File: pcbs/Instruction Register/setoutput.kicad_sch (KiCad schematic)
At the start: 9 parts, among them U3001 74HC245

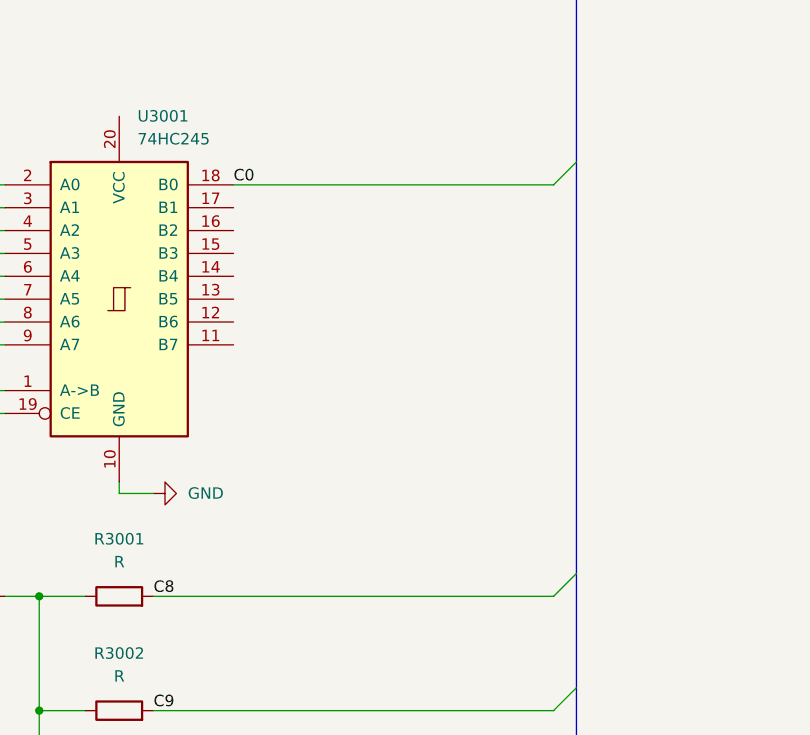
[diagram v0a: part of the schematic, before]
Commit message: Tweaking schematic and basic routing
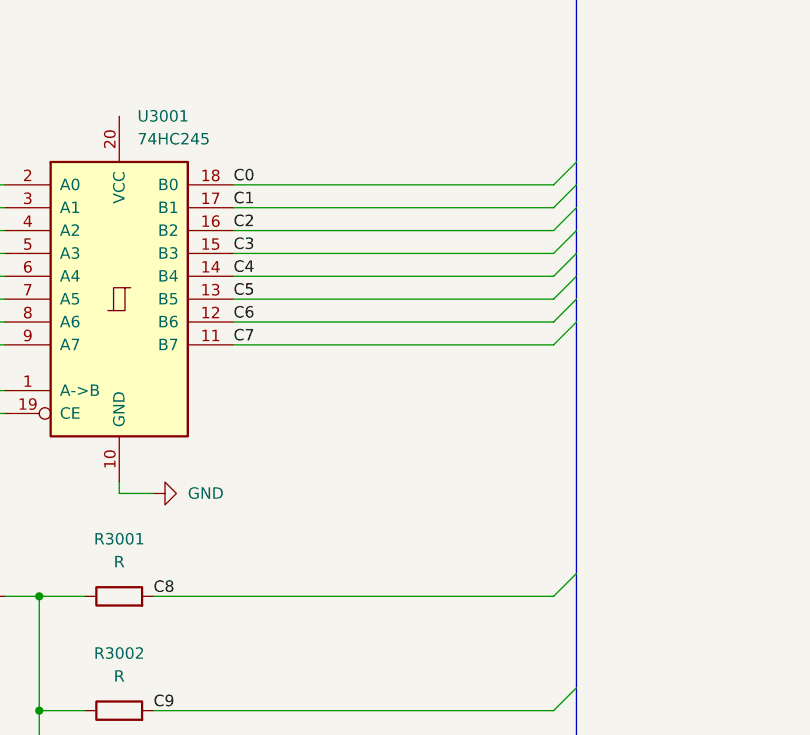
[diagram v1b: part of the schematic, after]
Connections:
- net C7: now reaches U3001.11 (B7)
- net C6: now reaches U3001.12 (B6)
- net C5: now reaches U3001.13 (B5)
- net C4: now reaches U3001.14 (B4)
- net C3: now reaches U3001.15 (B3)
- net C2: now reaches U3001.16 (B2)
- net C1: now reaches U3001.17 (B1)

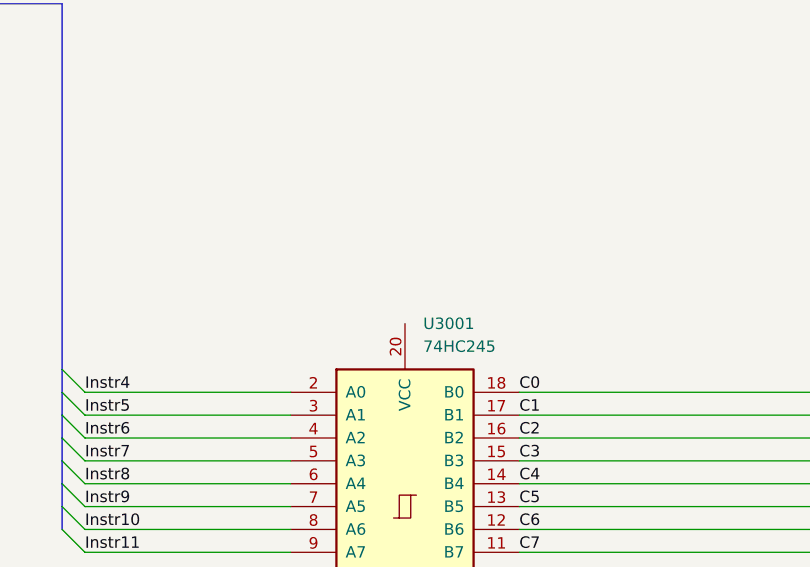
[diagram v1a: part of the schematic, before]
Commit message: Completing routing; needs silkscreen
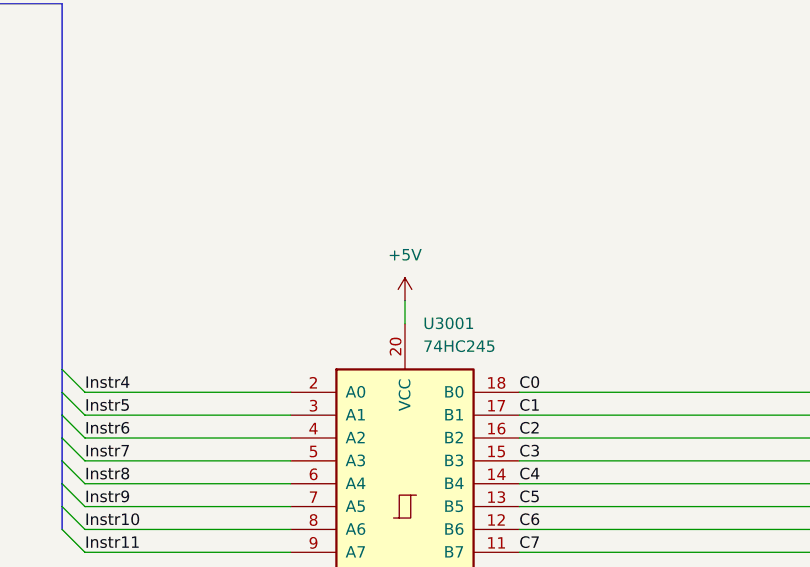
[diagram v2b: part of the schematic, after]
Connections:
- net +5V: now also U3001.20 (VCC)
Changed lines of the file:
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@@
+		)
+	)
+	(wire
+		(pts
+			(xy 127 83.82) (xy 127 86.36)
+		)
+		(stroke
+			(width 0)
+			(type default)
 		)
 	)
@@
 	(label "C4"
 		(at 139.7 104.14 0)
+		(fields_autoplaced yes)
 		(effects
 			(font
@@
 	(label "C5"
 		(at 139.7 106.68 0)
+		(fields_autoplaced yes)
 		(effects
 			(font
@@
 	(label "C2"
 		(at 139.7 99.06 0)
+		(fields_autoplaced yes)
 		(effects
 			(font
@@
 	(label "C1"
 		(at 139.7 96.52 0)
+		(fields_autoplaced yes)
 		(effects
 			(font
@@
 	(label "C3"
 		(at 139.7 101.6 0)
+		(fields_autoplaced yes)
 		(effects
 			(font
@@
 	(label "C7"
 		(at 139.7 111.76 0)
+		(fields_autoplaced yes)
 		(effects
 			(font
@@
 	(label "C6"
 		(at 139.7 109.22 0)
+		(fields_autoplaced yes)
 		(effects
 			(font
@@
 					(unit 1)
 				)
+			)
+		)
+	)
+	(symbol
+		(lib_id "power:+5V")
+		(at 127 83.82 0)
+		(unit 1)
+		(exclude_from_sim no)
+		(in_bom yes)
+		(on_board yes)
+		(dnp no)
+		(fields_autoplaced yes)
+		(property "Reference" "#PWR03004"
+			(at 127 87.63 0)
+			(effects
+				(font
+					(size 1.27 1.27)
+				)
+				(hide yes)
+			)
+		)
+		(property "Value" "+5V"
+			(at 127 78.74 0)
+			(effects
+				(font
+					(size 1.27 1.27)
+				)
+			)
+		)
+		(property "Footprint" ""
+			(at 127 83.82 0)
+			(effects
+				(font
+					(size 1.27 1.27)
+				)
+				(hide yes)
+			)
+		)
+		(property "Datasheet" ""
+			(at 127 83.82 0)
+			(effects
+				(font
+					(size 1.27 1.27)
+				)
+				(hide yes)
+			)
+		)
+		(property "Description" "Power symbol creates a global label with name \"+5V\""
+			(at 127 83.82 0)
+			(effects
+				(font
+					(size 1.27 1.27)
+				)
+				(hide yes)
+			)
+		)
+		(pin "1"
+		)
+		(instances
+			(project ""
+				(path "/dacc18b8-2bf2-4f24-ae04-b278bca3d46a/29957d29-df69-4b56-8517-df4781530091"
+					(reference "#PWR03004")
+					(unit 1)
+				)
